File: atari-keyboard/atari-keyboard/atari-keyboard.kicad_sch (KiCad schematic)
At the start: 158 parts, among them J101 I2C DISPLAY, J2 PLAYER 1, J3 PLAYER 2, SW1 MENU, SW10 1, SW11 2, SW12 3, SW13 4, SW14 5, SW15 6, SW16 7, SW17 8, SW18 UP, SW19 9, SW2 TURBO, SW20 0, SW21 <, SW22 >, SW23 BS, SW24 BRK, SW25 TAB, SW26 Q, SW27 DOWN, SW28 W, SW29 E, SW3 RESET, SW30 R, SW31 T, SW32 Y, SW33 U, SW34 I, SW35 O, SW36 LEFT, SW37 P, SW38 [-], SW39 [=], SW4 OPTION, SW40 RET, SW41 CTRL, SW42 A, SW43 S, SW44 D, SW45 RIGHT, SW46 F, SW47 G, SW48 H, SW49 J, SW5 SELECT, SW50 K, SW51 L, SW52 [;], SW53 [+], SW54 N, SW55 MULT, SW56 CAPS, SW57 LSHIFT, SW58 Z, SW59 X, SW6 START, SW60 C, SW61 V, SW62 B, SW63 M, SW64 FN, SW65 INV, SW66 SPC, SW67 [,], SW68 [.], SW69 [/], SW7 HELP, SW8 ESC, SW9 RSHIFT, U101 Elite-C

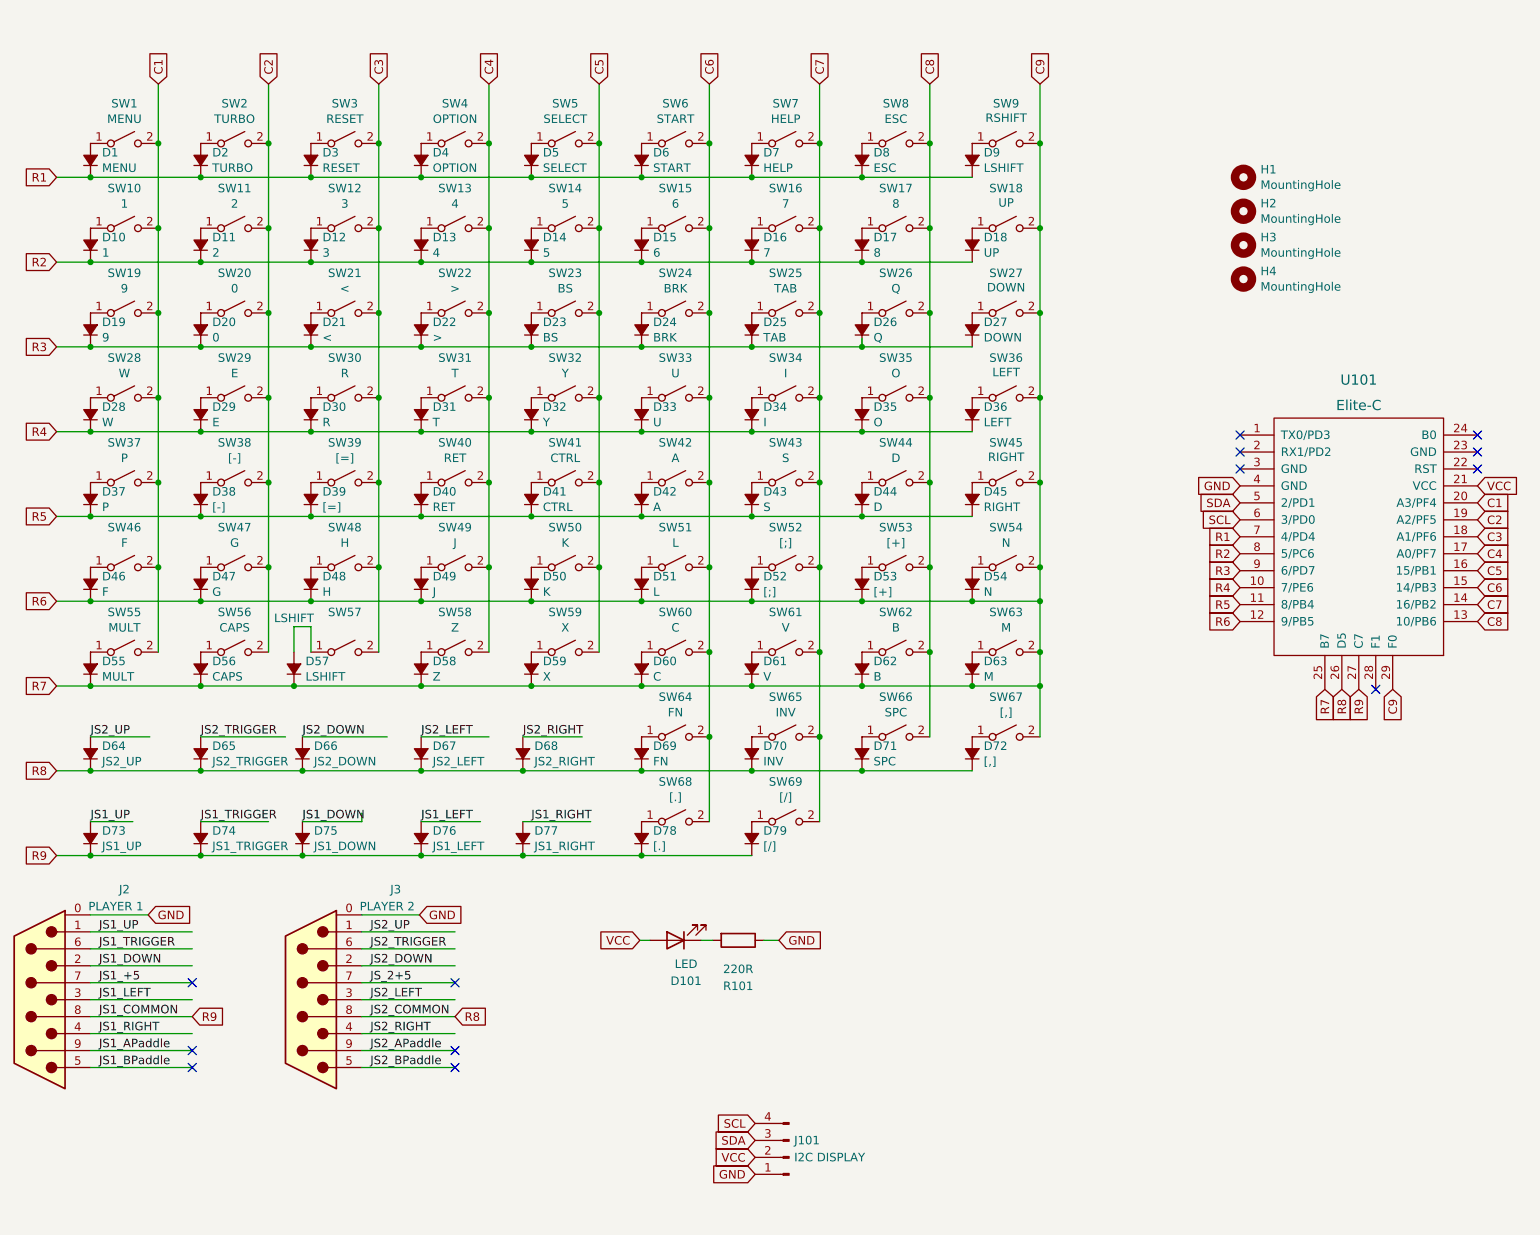
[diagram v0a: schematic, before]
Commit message: Cleaned up schematic
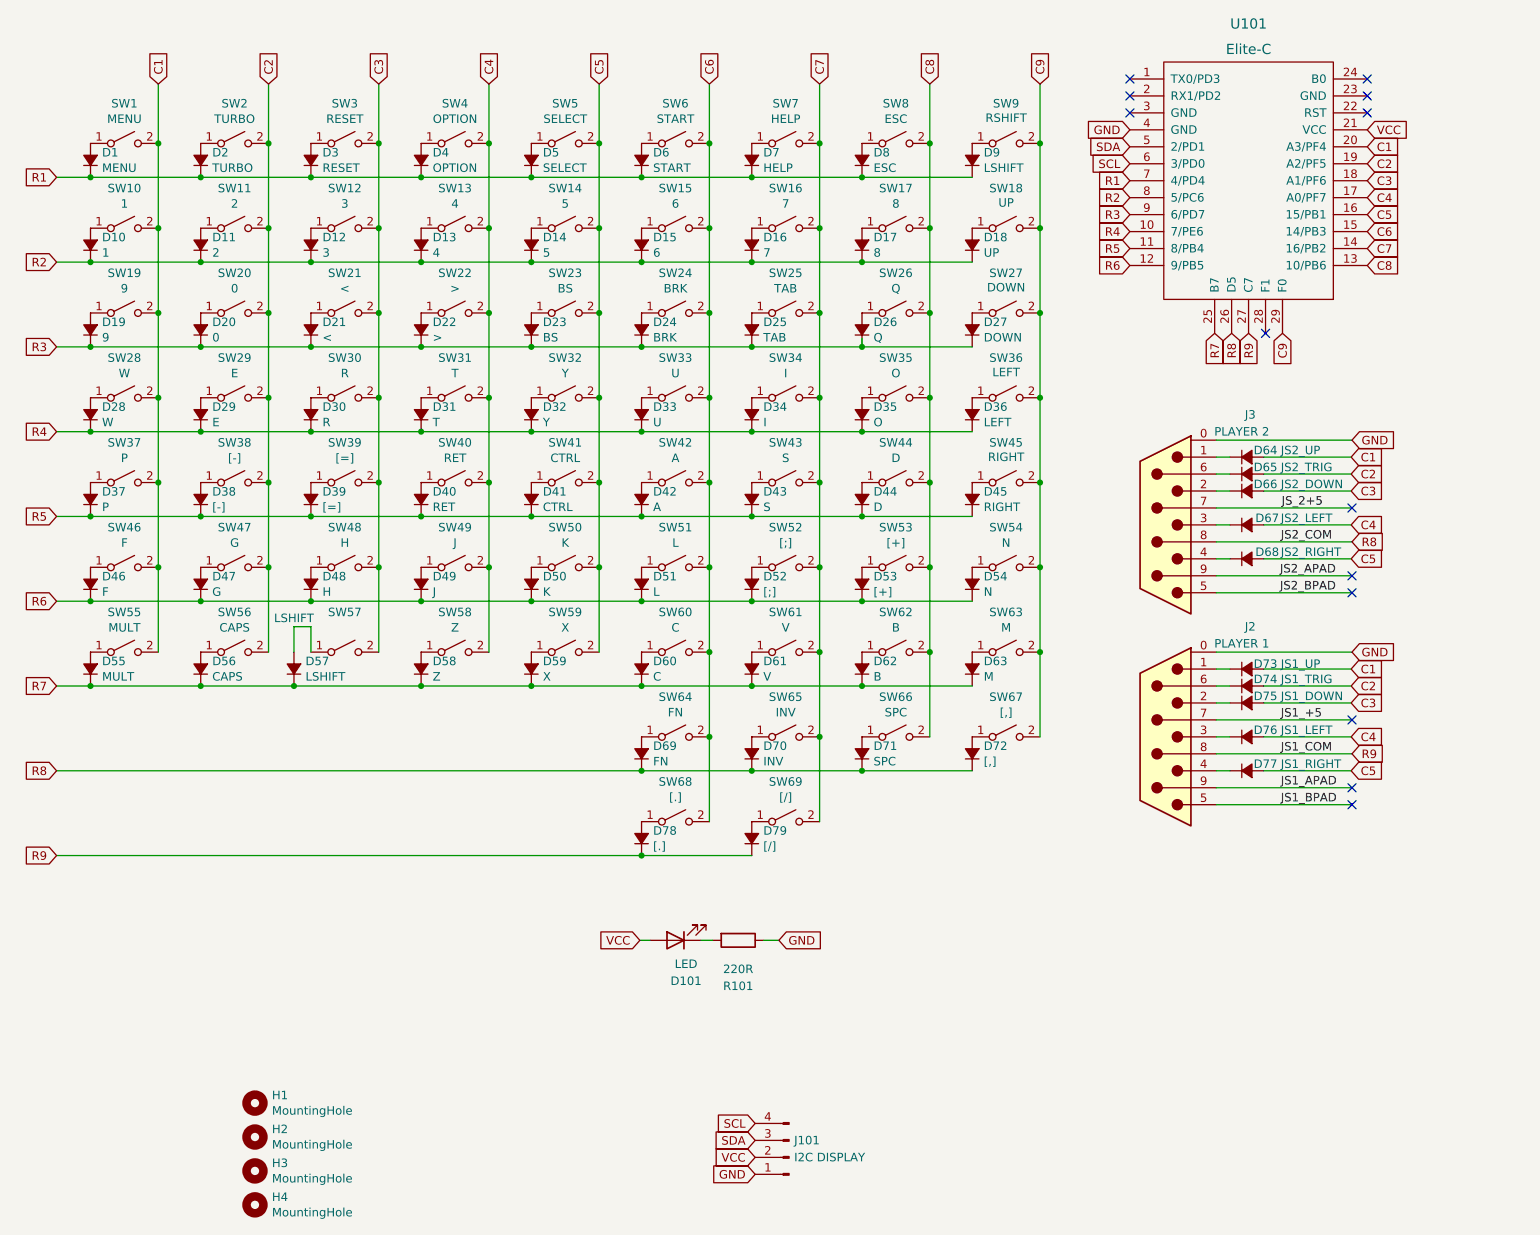
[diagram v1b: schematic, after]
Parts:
- D65: value JS2_TRIGGER -> JS2_TRIG
- D74: value JS1_TRIGGER -> JS1_TRIG
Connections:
- net C1: now also D64.2 (A), D73.2 (A)
- net C2: now also D65.2 (A), D74.2 (A)
- net C3: now also D66.2 (A), D75.2 (A)
- net C4: now also D67.2 (A), D76.2 (A)
- net C5: now also D68.2 (A), D77.2 (A)
- net C9: no longer D46.1 (K), D47.1 (K), D48.1 (K), D49.1 (K), D50.1 (K), D51.1 (K), D52.1 (K), D53.1 (K), D54.1 (K), D55.1 (K), D56.1 (K), D57.1 (K), D58.1 (K), D59.1 (K), D60.1 (K), D61.1 (K), D62.1 (K), D63.1 (K), U101.12 (9/PB5), U101.25 (B7)
- net R8: no longer D64.1 (K), D65.1 (K), D66.1 (K), D67.1 (K), D68.1 (K)
- net R9: no longer D73.1 (K), D74.1 (K), D75.1 (K), D76.1 (K), D77.1 (K)
- net JS1_APaddle renamed JS1_APAD
- net JS1_BPaddle renamed JS1_BPAD
- net JS1_DOWN: no longer names the net of J2.2
- net JS1_DOWN: now also D75.1 (K); no longer D75.2 (A)
- net JS1_LEFT: no longer names the net of J2.3
- net JS1_LEFT: now also D76.1 (K); no longer D76.2 (A)
- net JS1_RIGHT: no longer names the net of J2.4
- net JS1_RIGHT: now also D77.1 (K); no longer D77.2 (A)
- net JS1_TRIGGER: no longer names the net of J2.6
- net JS1_TRIGGER: now also D74.1 (K); no longer D74.2 (A)
- net JS1_UP: no longer names the net of J2.1
- net JS1_UP: now also D73.1 (K); no longer D73.2 (A)
- net JS2_APaddle renamed JS2_APAD
- net JS2_BPaddle renamed JS2_BPAD
- net JS2_DOWN: no longer names the net of J3.2
- net JS2_DOWN: now also D66.1 (K); no longer D66.2 (A)
- net JS2_LEFT: no longer names the net of J3.3
- net JS2_LEFT: now also D67.1 (K); no longer D67.2 (A)
- net JS2_RIGHT: no longer names the net of J3.4
- net JS2_RIGHT: now also D68.1 (K); no longer D68.2 (A)
- net JS2_TRIGGER: no longer names the net of J3.6
- net JS2_TRIGGER: now also D65.1 (K); no longer D65.2 (A)
- net JS2_UP: no longer names the net of J3.1
- net JS2_UP: now also D64.1 (K); no longer D64.2 (A)
- new net R6: D46.1 (K), D47.1 (K), D48.1 (K), D49.1 (K), D50.1 (K), D51.1 (K), D52.1 (K), D53.1 (K), D54.1 (K), U101.12 (9/PB5)
- new net R7: D55.1 (K), D56.1 (K), D57.1 (K), D58.1 (K), D59.1 (K), D60.1 (K), D61.1 (K), D62.1 (K), D63.1 (K), U101.25 (B7)
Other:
- moved on the sheet: D64, D65, D66, D67, D68, D73, D74, D75, D76, D77, H1, H2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

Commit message: Did the new keyboard layout.
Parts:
- removed D1: MENU, Diode_THT:D_A-405_P7.62mm_Horizontal, symbol atari-keyboard-rescue:D_Small_ALT-Device
- removed D10: 1, Diode_THT:D_A-405_P7.62mm_Horizontal, symbol atari-keyboard-rescue:D_Small_ALT-Device
- removed D11: 2, Diode_THT:D_A-405_P7.62mm_Horizontal, symbol atari-keyboard-rescue:D_Small_ALT-Device
- removed D12: 3, Diode_THT:D_A-405_P7.62mm_Horizontal, symbol atari-keyboard-rescue:D_Small_ALT-Device
- removed D13: 4, Diode_THT:D_A-405_P7.62mm_Horizontal, symbol atari-keyboard-rescue:D_Small_ALT-Device
- removed D14: 5, Diode_THT:D_A-405_P7.62mm_Horizontal, symbol atari-keyboard-rescue:D_Small_ALT-Device
- removed D15: 6, Diode_THT:D_A-405_P7.62mm_Horizontal, symbol atari-keyboard-rescue:D_Small_ALT-Device
- removed D16: 7, Diode_THT:D_A-405_P7.62mm_Horizontal, symbol atari-keyboard-rescue:D_Small_ALT-Device
- removed D17: 8, Diode_THT:D_A-405_P7.62mm_Horizontal, symbol atari-keyboard-rescue:D_Small_ALT-Device
- removed D18: UP, Diode_THT:D_A-405_P7.62mm_Horizontal, symbol atari-keyboard-rescue:D_Small_ALT-Device
- removed D19: 9, Diode_THT:D_A-405_P7.62mm_Horizontal, symbol atari-keyboard-rescue:D_Small_ALT-Device
- removed D2: TURBO, Diode_THT:D_A-405_P7.62mm_Horizontal, symbol atari-keyboard-rescue:D_Small_ALT-Device
- removed D20: 0, Diode_THT:D_A-405_P7.62mm_Horizontal, symbol atari-keyboard-rescue:D_Small_ALT-Device
- removed D21: <, Diode_THT:D_A-405_P7.62mm_Horizontal, symbol atari-keyboard-rescue:D_Small_ALT-Device
- removed D22: >, Diode_THT:D_A-405_P7.62mm_Horizontal, symbol atari-keyboard-rescue:D_Small_ALT-Device
- removed D23: BS, Diode_THT:D_A-405_P7.62mm_Horizontal, symbol atari-keyboard-rescue:D_Small_ALT-Device
- removed D24: BRK, Diode_THT:D_A-405_P7.62mm_Horizontal, symbol atari-keyboard-rescue:D_Small_ALT-Device
- removed D25: TAB, Diode_THT:D_A-405_P7.62mm_Horizontal, symbol atari-keyboard-rescue:D_Small_ALT-Device
- removed D26: Q, Diode_THT:D_A-405_P7.62mm_Horizontal, symbol atari-keyboard-rescue:D_Small_ALT-Device
- removed D27: DOWN, Diode_THT:D_A-405_P7.62mm_Horizontal, symbol atari-keyboard-rescue:D_Small_ALT-Device
- removed D28: W, Diode_THT:D_A-405_P7.62mm_Horizontal, symbol atari-keyboard-rescue:D_Small_ALT-Device
- removed D29: E, Diode_THT:D_A-405_P7.62mm_Horizontal, symbol atari-keyboard-rescue:D_Small_ALT-Device
- removed D3: RESET, Diode_THT:D_A-405_P7.62mm_Horizontal, symbol atari-keyboard-rescue:D_Small_ALT-Device
- removed D30: R, Diode_THT:D_A-405_P7.62mm_Horizontal, symbol atari-keyboard-rescue:D_Small_ALT-Device
- removed D31: T, Diode_THT:D_A-405_P7.62mm_Horizontal, symbol atari-keyboard-rescue:D_Small_ALT-Device
- removed D32: Y, Diode_THT:D_A-405_P7.62mm_Horizontal, symbol atari-keyboard-rescue:D_Small_ALT-Device
- removed D33: U, Diode_THT:D_A-405_P7.62mm_Horizontal, symbol atari-keyboard-rescue:D_Small_ALT-Device
- removed D34: I, Diode_THT:D_A-405_P7.62mm_Horizontal, symbol atari-keyboard-rescue:D_Small_ALT-Device
- removed D35: O, Diode_THT:D_A-405_P7.62mm_Horizontal, symbol atari-keyboard-rescue:D_Small_ALT-Device
- removed D36: LEFT, Diode_THT:D_A-405_P7.62mm_Horizontal, symbol atari-keyboard-rescue:D_Small_ALT-Device
- removed D37: P, Diode_THT:D_A-405_P7.62mm_Horizontal, symbol atari-keyboard-rescue:D_Small_ALT-Device
- removed D38: [-], Diode_THT:D_A-405_P7.62mm_Horizontal, symbol atari-keyboard-rescue:D_Small_ALT-Device
- removed D39: [=], Diode_THT:D_A-405_P7.62mm_Horizontal, symbol atari-keyboard-rescue:D_Small_ALT-Device
- removed D4: OPTION, Diode_THT:D_A-405_P7.62mm_Horizontal, symbol atari-keyboard-rescue:D_Small_ALT-Device
- removed D40: RET, Diode_THT:D_A-405_P7.62mm_Horizontal, symbol atari-keyboard-rescue:D_Small_ALT-Device
- removed D41: CTRL, Diode_THT:D_A-405_P7.62mm_Horizontal, symbol atari-keyboard-rescue:D_Small_ALT-Device
- removed D42: A, Diode_THT:D_A-405_P7.62mm_Horizontal, symbol atari-keyboard-rescue:D_Small_ALT-Device
- removed D43: S, Diode_THT:D_A-405_P7.62mm_Horizontal, symbol atari-keyboard-rescue:D_Small_ALT-Device
- removed D44: D, Diode_THT:D_A-405_P7.62mm_Horizontal, symbol atari-keyboard-rescue:D_Small_ALT-Device
- removed D45: RIGHT, Diode_THT:D_A-405_P7.62mm_Horizontal, symbol atari-keyboard-rescue:D_Small_ALT-Device
- removed D46: F, Diode_THT:D_A-405_P7.62mm_Horizontal, symbol atari-keyboard-rescue:D_Small_ALT-Device
- removed D47: G, Diode_THT:D_A-405_P7.62mm_Horizontal, symbol atari-keyboard-rescue:D_Small_ALT-Device
- removed D48: H, Diode_THT:D_A-405_P7.62mm_Horizontal, symbol atari-keyboard-rescue:D_Small_ALT-Device
- removed D49: J, Diode_THT:D_A-405_P7.62mm_Horizontal, symbol atari-keyboard-rescue:D_Small_ALT-Device
- removed D5: SELECT, Diode_THT:D_A-405_P7.62mm_Horizontal, symbol atari-keyboard-rescue:D_Small_ALT-Device
- removed D50: K, Diode_THT:D_A-405_P7.62mm_Horizontal, symbol atari-keyboard-rescue:D_Small_ALT-Device
- removed D51: L, Diode_THT:D_A-405_P7.62mm_Horizontal, symbol atari-keyboard-rescue:D_Small_ALT-Device
- removed D52: [;], Diode_THT:D_A-405_P7.62mm_Horizontal, symbol atari-keyboard-rescue:D_Small_ALT-Device
- removed D53: [+], Diode_THT:D_A-405_P7.62mm_Horizontal, symbol atari-keyboard-rescue:D_Small_ALT-Device
- removed D54: N, Diode_THT:D_A-405_P7.62mm_Horizontal, symbol atari-keyboard-rescue:D_Small_ALT-Device
- removed D55: MULT, Diode_THT:D_A-405_P7.62mm_Horizontal, symbol atari-keyboard-rescue:D_Small_ALT-Device
- removed D56: CAPS, Diode_THT:D_A-405_P7.62mm_Horizontal, symbol atari-keyboard-rescue:D_Small_ALT-Device
- removed D57, D9: LSHIFT, Diode_THT:D_A-405_P7.62mm_Horizontal, symbol atari-keyboard-rescue:D_Small_ALT-Device
- removed D58: Z, Diode_THT:D_A-405_P7.62mm_Horizontal, symbol atari-keyboard-rescue:D_Small_ALT-Device
- removed D59: X, Diode_THT:D_A-405_P7.62mm_Horizontal, symbol atari-keyboard-rescue:D_Small_ALT-Device
- removed D6: START, Diode_THT:D_A-405_P7.62mm_Horizontal, symbol atari-keyboard-rescue:D_Small_ALT-Device
- removed D60: C, Diode_THT:D_A-405_P7.62mm_Horizontal, symbol atari-keyboard-rescue:D_Small_ALT-Device
- removed D61: V, Diode_THT:D_A-405_P7.62mm_Horizontal, symbol atari-keyboard-rescue:D_Small_ALT-Device
- removed D62: B, Diode_THT:D_A-405_P7.62mm_Horizontal, symbol atari-keyboard-rescue:D_Small_ALT-Device
- removed D63: M, Diode_THT:D_A-405_P7.62mm_Horizontal, symbol atari-keyboard-rescue:D_Small_ALT-Device
- removed D69: FN, Diode_THT:D_A-405_P7.62mm_Horizontal, symbol atari-keyboard-rescue:D_Small_ALT-Device
- removed D7: HELP, Diode_THT:D_A-405_P7.62mm_Horizontal, symbol atari-keyboard-rescue:D_Small_ALT-Device
- removed D70: INV, Diode_THT:D_A-405_P7.62mm_Horizontal, symbol atari-keyboard-rescue:D_Small_ALT-Device
- removed D71: SPC, Diode_THT:D_A-405_P7.62mm_Horizontal, symbol atari-keyboard-rescue:D_Small_ALT-Device
- removed D72: [,], Diode_THT:D_A-405_P7.62mm_Horizontal, symbol atari-keyboard-rescue:D_Small_ALT-Device
- removed D78: [.], Diode_THT:D_A-405_P7.62mm_Horizontal, symbol atari-keyboard-rescue:D_Small_ALT-Device
- removed D79: [/], Diode_THT:D_A-405_P7.62mm_Horizontal, symbol atari-keyboard-rescue:D_Small_ALT-Device
- removed D8: ESC, Diode_THT:D_A-405_P7.62mm_Horizontal, symbol atari-keyboard-rescue:D_Small_ALT-Device
- removed SW1: MENU, Button_Switch_Keyboard:SW_Cherry_MX_1.00u_PCB, symbol Switch:SW_SPST
- removed SW10: 1, Button_Switch_Keyboard:SW_Cherry_MX_1.00u_PCB, symbol Switch:SW_SPST
- removed SW11: 2, Button_Switch_Keyboard:SW_Cherry_MX_1.00u_PCB, symbol Switch:SW_SPST
- removed SW12: 3, Button_Switch_Keyboard:SW_Cherry_MX_1.00u_PCB, symbol Switch:SW_SPST
- removed SW13: 4, Button_Switch_Keyboard:SW_Cherry_MX_1.00u_PCB, symbol Switch:SW_SPST
- removed SW14: 5, Button_Switch_Keyboard:SW_Cherry_MX_1.00u_PCB, symbol Switch:SW_SPST
- removed SW15: 6, Button_Switch_Keyboard:SW_Cherry_MX_1.00u_PCB, symbol Switch:SW_SPST
- removed SW16: 7, Button_Switch_Keyboard:SW_Cherry_MX_1.00u_PCB, symbol Switch:SW_SPST
- removed SW17: 8, Button_Switch_Keyboard:SW_Cherry_MX_1.00u_PCB, symbol Switch:SW_SPST
- removed SW18: UP, Button_Switch_Keyboard:SW_Cherry_MX_1.00u_PCB, symbol Switch:SW_SPST
- removed SW19: 9, Button_Switch_Keyboard:SW_Cherry_MX_1.00u_PCB, symbol Switch:SW_SPST
- removed SW2: TURBO, Button_Switch_Keyboard:SW_Cherry_MX_1.00u_PCB, symbol Switch:SW_SPST
- removed SW20: 0, Button_Switch_Keyboard:SW_Cherry_MX_1.00u_PCB, symbol Switch:SW_SPST
- removed SW21: <, Button_Switch_Keyboard:SW_Cherry_MX_1.00u_PCB, symbol Switch:SW_SPST
- removed SW22: >, Button_Switch_Keyboard:SW_Cherry_MX_1.00u_PCB, symbol Switch:SW_SPST
- removed SW23: BS, Button_Switch_Keyboard:SW_Cherry_MX_2.00u_PCB, symbol Switch:SW_SPST
- removed SW24: BRK, Button_Switch_Keyboard:SW_Cherry_MX_1.00u_PCB, symbol Switch:SW_SPST
- removed SW25: TAB, Button_Switch_Keyboard:SW_Cherry_MX_1.75u_PCB, symbol Switch:SW_SPST
- removed SW26: Q, Button_Switch_Keyboard:SW_Cherry_MX_1.00u_PCB, symbol Switch:SW_SPST
- removed SW27: DOWN, Button_Switch_Keyboard:SW_Cherry_MX_1.00u_PCB, symbol Switch:SW_SPST
- removed SW28: W, Button_Switch_Keyboard:SW_Cherry_MX_1.00u_PCB, symbol Switch:SW_SPST
- removed SW29: E, Button_Switch_Keyboard:SW_Cherry_MX_1.00u_PCB, symbol Switch:SW_SPST
- removed SW3: RESET, Button_Switch_Keyboard:SW_Cherry_MX_1.00u_PCB, symbol Switch:SW_SPST
- removed SW30: R, Button_Switch_Keyboard:SW_Cherry_MX_1.00u_PCB, symbol Switch:SW_SPST
- removed SW31: T, Button_Switch_Keyboard:SW_Cherry_MX_1.00u_PCB, symbol Switch:SW_SPST
- removed SW32: Y, Button_Switch_Keyboard:SW_Cherry_MX_1.00u_PCB, symbol Switch:SW_SPST
- removed SW33: U, Button_Switch_Keyboard:SW_Cherry_MX_1.00u_PCB, symbol Switch:SW_SPST
- removed SW34: I, Button_Switch_Keyboard:SW_Cherry_MX_1.00u_PCB, symbol Switch:SW_SPST
- removed SW35: O, Button_Switch_Keyboard:SW_Cherry_MX_1.00u_PCB, symbol Switch:SW_SPST
- removed SW36: LEFT, Button_Switch_Keyboard:SW_Cherry_MX_1.00u_PCB, symbol Switch:SW_SPST
- removed SW37: P, Button_Switch_Keyboard:SW_Cherry_MX_1.00u_PCB, symbol Switch:SW_SPST
- removed SW38: [-], Button_Switch_Keyboard:SW_Cherry_MX_1.00u_PCB, symbol Switch:SW_SPST
- removed SW39: [=], Button_Switch_Keyboard:SW_Cherry_MX_1.00u_PCB, symbol Switch:SW_SPST
- removed SW4: OPTION, Button_Switch_Keyboard:SW_Cherry_MX_1.00u_PCB, symbol Switch:SW_SPST
- removed SW40: RET, Button_Switch_Keyboard:SW_Cherry_MX_1.50u_PCB, symbol Switch:SW_SPST
- removed SW41: CTRL, Button_Switch_Keyboard:SW_Cherry_MX_2.00u_PCB, symbol Switch:SW_SPST
- removed SW42: A, Button_Switch_Keyboard:SW_Cherry_MX_1.00u_PCB, symbol Switch:SW_SPST
- removed SW43: S, Button_Switch_Keyboard:SW_Cherry_MX_1.00u_PCB, symbol Switch:SW_SPST
- removed SW44: D, Button_Switch_Keyboard:SW_Cherry_MX_1.00u_PCB, symbol Switch:SW_SPST
- removed SW45: RIGHT, Button_Switch_Keyboard:SW_Cherry_MX_1.00u_PCB, symbol Switch:SW_SPST
- removed SW46: F, Button_Switch_Keyboard:SW_Cherry_MX_1.00u_PCB, symbol Switch:SW_SPST
- removed SW47: G, Button_Switch_Keyboard:SW_Cherry_MX_1.00u_PCB, symbol Switch:SW_SPST
- removed SW48: H, Button_Switch_Keyboard:SW_Cherry_MX_1.00u_PCB, symbol Switch:SW_SPST
- removed SW49: J, Button_Switch_Keyboard:SW_Cherry_MX_1.00u_PCB, symbol Switch:SW_SPST
- removed SW5: SELECT, Button_Switch_Keyboard:SW_Cherry_MX_1.00u_PCB, symbol Switch:SW_SPST
- removed SW50: K, Button_Switch_Keyboard:SW_Cherry_MX_1.00u_PCB, symbol Switch:SW_SPST
- removed SW51: L, Button_Switch_Keyboard:SW_Cherry_MX_1.00u_PCB, symbol Switch:SW_SPST
- removed SW52: [;], Button_Switch_Keyboard:SW_Cherry_MX_1.00u_PCB, symbol Switch:SW_SPST
- removed SW53: [+], Button_Switch_Keyboard:SW_Cherry_MX_1.00u_PCB, symbol Switch:SW_SPST
- removed SW54: N, Button_Switch_Keyboard:SW_Cherry_MX_1.00u_PCB, symbol Switch:SW_SPST
- removed SW55: MULT, Button_Switch_Keyboard:SW_Cherry_MX_1.00u_PCB, symbol Switch:SW_SPST
- removed SW56: CAPS, Button_Switch_Keyboard:SW_Cherry_MX_1.25u_PCB, symbol Switch:SW_SPST
- removed SW57: LSHIFT, Button_Switch_Keyboard:SW_Cherry_MX_2.25u_PCB, symbol Switch:SW_SPST
- removed SW58: Z, Button_Switch_Keyboard:SW_Cherry_MX_1.00u_PCB, symbol Switch:SW_SPST
- removed SW59: X, Button_Switch_Keyboard:SW_Cherry_MX_1.00u_PCB, symbol Switch:SW_SPST
- removed SW6: START, Button_Switch_Keyboard:SW_Cherry_MX_1.00u_PCB, symbol Switch:SW_SPST
- removed SW60: C, Button_Switch_Keyboard:SW_Cherry_MX_1.00u_PCB, symbol Switch:SW_SPST
- removed SW61: V, Button_Switch_Keyboard:SW_Cherry_MX_1.00u_PCB, symbol Switch:SW_SPST
- removed SW62: B, Button_Switch_Keyboard:SW_Cherry_MX_1.00u_PCB, symbol Switch:SW_SPST
- removed SW63: M, Button_Switch_Keyboard:SW_Cherry_MX_1.00u_PCB, symbol Switch:SW_SPST
- removed SW64: FN, Button_Switch_Keyboard:SW_Cherry_MX_1.75u_PCB, symbol Switch:SW_SPST
- removed SW65: INV, Button_Switch_Keyboard:SW_Cherry_MX_1.00u_PCB, symbol Switch:SW_SPST
- removed SW66: SPC, Button_Switch_Keyboard:SW_Cherry_MX_6.25u_PCB, symbol Switch:SW_SPST
- removed SW67: [,], Button_Switch_Keyboard:SW_Cherry_MX_1.00u_PCB, symbol Switch:SW_SPST
- removed SW68: [.], Button_Switch_Keyboard:SW_Cherry_MX_1.00u_PCB, symbol Switch:SW_SPST
- removed SW69: [/], Button_Switch_Keyboard:SW_Cherry_MX_1.00u_PCB, symbol Switch:SW_SPST
- removed SW7: HELP, Button_Switch_Keyboard:SW_Cherry_MX_1.00u_PCB, symbol Switch:SW_SPST
- removed SW8: ESC, Button_Switch_Keyboard:SW_Cherry_MX_1.25u_PCB, symbol Switch:SW_SPST
- removed SW9: RSHIFT, Button_Switch_Keyboard:SW_Cherry_MX_1.75u_PCB, symbol Switch:SW_SPST
- renumbered D64 to D101, D65 to D102, D66 to D103, D67 to D104, D68 to D105, D73 to D106, D74 to D107, D75 to D108, D76 to D109, D77 to D110, D101 to D111, H1 to H101, H2 to H102, H3 to H103, H4 to H104, J3 to J101, J2 to J102, J101 to J103
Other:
- added sheet Keyboard Matrix (keyboard.kicad_sch)
- note added: "The keyboard matrix is in its own sheet so that the switch refs and diode refs will keep a 1:1 relationship. This makes it easier for tools that automatically place the keys to find what they are looking for."

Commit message: Switched over to hybrid resisters and diodes.
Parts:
- D101, D102, D103, D104, D105, D106, D107, D108, D109, D110: footprint Diode_THT:D_A-405_P7.62mm_Horizontal -> keebio:Diode-dual
- R101: footprint Resistor_THT:R_Axial_DIN0204_L3.6mm_D1.6mm_P5.08mm_Horizontal -> keebio:Resistor-Hybrid

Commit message: mounting holes in place
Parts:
- D102, D103, D104, D105, D106, D107, D108, D109, D110: footprint keebio:Diode-dual -> retro-kbd:Diode-dual

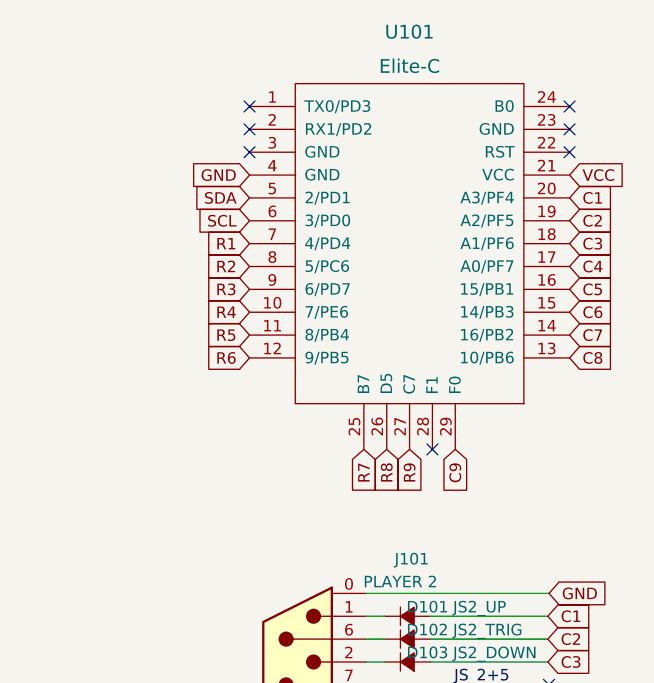
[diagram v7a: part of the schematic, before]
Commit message: Exclusion zones and board routed.
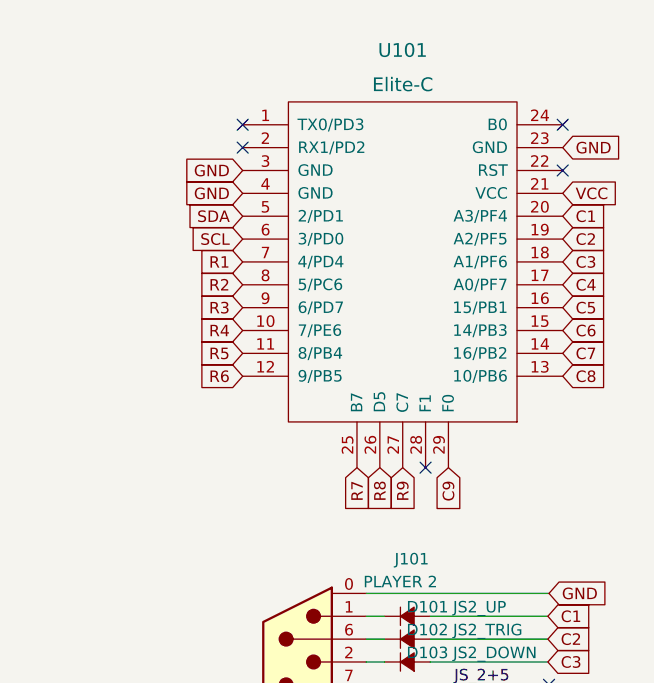
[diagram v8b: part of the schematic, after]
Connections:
- net GND: now also U101.23 (GND), U101.3 (GND)
- no-connect marks 13 -> 11
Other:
- moved on the sheet: U101
